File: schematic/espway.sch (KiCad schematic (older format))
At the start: 18 parts, among them M1 motor, M2 motor, U1 WS2812B, U2 AMS1117-5.0, U3 GY-521, U4 WS2812B, U5 WEMOS D1 mini, U6 L293D

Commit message: Add new schematic, update file structure and README
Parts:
- removed C1: 100n, symbol C
- removed C2: 1000u, symbol CP
- removed M1, M2: motor, symbol motor
- removed U1, U4: WS2812B, symbol ws2812b
- removed U2: AMS1117-5.0, symbol LM1117-5.0
- removed U3: GY-521, symbol GY-521
- removed U5: WEMOS D1 mini, symbol d1_mini
- removed U6: L293D, symbol L293D
- added BT1: 4.8V (4*AAA NiMH), symbol Battery
- added C1: 470u, symbol CP
- added C2: 100n, symbol C
- added J1, J2: CONN_01X02, symbol CONN_01X02
- added J3: CONN_01X04_MALE, symbol CONN_01X04_MALE
- added L1: Ferrite_Bead, symbol Ferrite_Bead
- added R10, R5, R6, R7, R8: 10k, symbol R
- added R11, R4: 470, symbol R
- added R9: 82k, symbol R
- added SW1: SW_Push, symbol SW_Push
- added U1: DRV8835, symbol DRV8835
- added U2: LM1117-3.3, symbol LM1117-3.3
- added U3: ESP-12E, symbol ESP-12E
- added U4: LSM6DS3, symbol LSM6DS3
- C5: value 1000u -> 100u
- R1: value 470 -> 10k
- R2: value 680k -> 10k
- R3: value 10k -> 470
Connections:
- net labels added: +3.3V, ADC, GPIO15, INT, SCL, SDA
- net labels removed: +5V, 1Y, 2Y, 3A, 4A
- wire segments 74 -> 72
- no-connect marks 1 -> 0
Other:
- note removed: "C6, C7 close to the motors\nMotor wires should be twisted pairs and as short as possible\nC1 close to U1 and U4\nC3, C4 close to U2\nC5 close to U5, C2 close to U6\nKeep wires between U3 and U5 short"

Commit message: Add kicad net file, begin associating footprints
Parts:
- BT1: footprint (none) -> Wire_Pads:SolderWirePad_2x_1-5mmDrill
- C1: footprint (none) -> Capacitors_SMD:CP_Elec_8x10
- C2, C3, C4, C6, C7: footprint (none) -> Capacitors_SMD:C_0603
- J3: footprint (none) -> Pin_Headers:Pin_Header_Angled_1x04_Pitch2.54mm
- L1: footprint (none) -> Inductors_SMD:L_0603
- R1, R10, R11, R2, R3, R4, R5, R6, R7, R8, R9: footprint (none) -> Resistors_SMD:R_0603
- U2: footprint (none) -> TO_SOT_Packages_SMD:SOT-223
- U3: footprint (none) -> ESP8266:ESP-12E_SMD
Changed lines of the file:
@@
 F 0 "U3" H 6200 2550 50  0000 C CNN
 F 1 "ESP-12E" H 6200 2750 50  0000 C CNN
-F 2 "" H 6200 2650 50  0001 C CNN
+F 2 "ESP8266:ESP-12E_SMD" H 6200 2650 50  0001 C CNN
 F 3 "" H 6200 2650 50  0001 C CNN
 	1    6200 2650
@@
 $EndComp
 $Comp
-L GND #PWR8
+L GND #PWR01
 U 1 1 59B6CE9D
 P 7450 3850
-F 0 "#PWR8" H 7450 3600 50  0001 C CNN
+F 0 "#PWR01" H 7450 3600 50  0001 C CNN
 F 1 "GND" H 7450 3700 50  0000 C CNN
 F 2 "" H 7450 3850 50  0001 C CNN
@@
 F 0 "R6" V 7530 3450 50  0000 C CNN
 F 1 "10k" V 7450 3450 50  0000 C CNN
-F 2 "" V 7380 3450 50  0001 C CNN
+F 2 "Resistors_SMD:R_0603" V 7380 3450 50  0001 C CNN
 F 3 "" H 7450 3450 50  0001 C CNN
 	1    7450 3450
@@
 F 0 "C4" H 5325 3550 50  0000 L CNN
 F 1 "100n" H 5325 3350 50  0000 L CNN
-F 2 "" H 5338 3300 50  0001 C CNN
+F 2 "Capacitors_SMD:C_0603" H 5338 3300 50  0001 C CNN
 F 3 "" H 5300 3450 50  0001 C CNN
 	1    5300 3450
@@
 F 0 "R3" V 7150 2300 50  0000 C CNN
 F 1 "470" V 7250 2350 50  0000 C CNN
-F 2 "" V 7180 2350 50  0001 C CNN
+F 2 "Resistors_SMD:R_0603" V 7180 2350 50  0001 C CNN
 F 3 "" H 7250 2350 50  0001 C CNN
 	1    7250 2350
@@
 F 0 "R4" V 7350 2600 50  0000 C CNN
 F 1 "470" V 7250 2450 50  0000 C CNN
-F 2 "" V 7180 2450 50  0001 C CNN
+F 2 "Resistors_SMD:R_0603" V 7180 2450 50  0001 C CNN
 F 3 "" H 7250 2450 50  0001 C CNN
 	1    7250 2450
@@
 F 0 "R1" V 5130 2350 50  0000 C CNN
 F 1 "10k" V 5050 2350 50  0000 C CNN
-F 2 "" V 4980 2350 50  0001 C CNN
+F 2 "Resistors_SMD:R_0603" V 4980 2350 50  0001 C CNN
 F 3 "" H 5050 2350 50  0001 C CNN
 	1    5050 2350
@@
 $EndComp
 $Comp
-L +3.3V #PWR4
+L +3.3V #PWR02
 U 1 1 59B80453
 P 4900 2250
-F 0 "#PWR4" H 4900 2100 50  0001 C CNN
+F 0 "#PWR02" H 4900 2100 50  0001 C CNN
 F 1 "+3.3V" H 4900 2390 50  0000 C CNN
 F 2 "" H 4900 2250 50  0001 C CNN
@@
 F 0 "R2" V 5130 2550 50  0000 C CNN
 F 1 "10k" V 5050 2550 50  0000 C CNN
-F 2 "" V 4980 2550 50  0001 C CNN
+F 2 "Resistors_SMD:R_0603" V 4980 2550 50  0001 C CNN
 F 3 "" H 5050 2550 50  0001 C CNN
 	1    5050 2550
@@
 F 0 "R9" V 9230 2200 50  0000 C CNN
 F 1 "82k" V 9150 2200 50  0000 C CNN
-F 2 "" V 9080 2200 50  0001 C CNN
+F 2 "Resistors_SMD:R_0603" V 9080 2200 50  0001 C CNN
 F 3 "" H 9150 2200 50  0001 C CNN
 	1    9150 2200
@@
 F 0 "R10" V 9230 2600 50  0000 C CNN
 F 1 "10k" V 9150 2600 50  0000 C CNN
-F 2 "" V 9080 2600 50  0001 C CNN
+F 2 "Resistors_SMD:R_0603" V 9080 2600 50  0001 C CNN
 F 3 "" H 9150 2600 50  0001 C CNN
 	1    9150 2600
@@
 $EndComp
 $Comp
-L GND #PWR15
+L GND #PWR03
 U 1 1 59B809EC
 P 9150 2850
-F 0 "#PWR15" H 9150 2600 50  0001 C CNN
+F 0 "#PWR03" H 9150 2600 50  0001 C CNN
 F 1 "GND" H 9150 2700 50  0000 C CNN
 F 2 "" H 9150 2850 50  0001 C CNN
@@
 SDA
 $Comp
-L +3.3V #PWR13
+L +3.3V #PWR04
 U 1 1 59B80D23
 P 8800 4000
-F 0 "#PWR13" H 8800 3850 50  0001 C CNN
+F 0 "#PWR04" H 8800 3850 50  0001 C CNN
 F 1 "+3.3V" H 8800 4140 50  0000 C CNN
 F 2 "" H 8800 4000 50  0001 C CNN
@@
 F 0 "R7" V 8880 4150 50  0000 C CNN
 F 1 "10k" V 8800 4150 50  0000 C CNN
-F 2 "" V 8730 4150 50  0001 C CNN
+F 2 "Resistors_SMD:R_0603" V 8730 4150 50  0001 C CNN
 F 3 "" H 8800 4150 50  0001 C CNN
 	1    8800 4150
@@
 F 0 "R8" V 9080 4150 50  0000 C CNN
 F 1 "10k" V 9000 4150 50  0000 C CNN
-F 2 "" V 8930 4150 50  0001 C CNN
+F 2 "Resistors_SMD:R_0603" V 8930 4150 50  0001 C CNN
 F 3 "" H 9000 4150 50  0001 C CNN
 	1    9000 4150
@@
 SDA
 $Comp
-L GND #PWR11
+L GND #PWR05
 U 1 1 59B8139A
 P 8050 2750
-F 0 "#PWR11" H 8050 2500 50  0001 C CNN
+F 0 "#PWR05" H 8050 2500 50  0001 C CNN
 F 1 "GND" H 8050 2600 50  0000 C CNN
 F 2 "" H 8050 2750 50  0001 C CNN
@@
 F 0 "R11" V 9580 4550 50  0000 C CNN
 F 1 "470" V 9500 4550 50  0000 C CNN
-F 2 "" V 9430 4550 50  0001 C CNN
+F 2 "Resistors_SMD:R_0603" V 9430 4550 50  0001 C CNN
 F 3 "" H 9500 4550 50  0001 C CNN
 	1    9500 4550
@@
 F 0 "U2" H 5950 950 50  0000 C CNN
 F 1 "LM1117-3.3" H 5850 1450 50  0000 C CNN
-F 2 "" H 5850 1200 50  0001 C CNN
+F 2 "TO_SOT_Packages_SMD:SOT-223" H 5850 1200 50  0001 C CNN
 F 3 "" H 5850 1200 50  0001 C CNN
 	1    5850 1200
@@
 $EndComp
 $Comp
-L GND #PWR6
+L GND #PWR06
 U 1 1 59B829FA
 P 5850 1600
-F 0 "#PWR6" H 5850 1350 50  0001 C CNN
+F 0 "#PWR06" H 5850 1350 50  0001 C CNN
 F 1 "GND" H 5850 1450 50  0000 C CNN
 F 2 "" H 5850 1600 50  0001 C CNN
@@
 $EndComp
 $Comp
-L +3.3V #PWR7
+L +3.3V #PWR07
 U 1 1 59B82E61
 P 6300 1200
-F 0 "#PWR7" H 6300 1050 50  0001 C CNN
+F 0 "#PWR07" H 6300 1050 50  0001 C CNN
 F 1 "+3.3V" H 6300 1340 50  0000 C CNN
 F 2 "" H 6300 1200 50  0001 C CNN
@@
 F 0 "C6" H 8275 5900 50  0000 L CNN
 F 1 "100n" H 8275 5700 50  0000 L CNN
-F 2 "" H 8288 5650 50  0001 C CNN
+F 2 "Capacitors_SMD:C_0603" H 8288 5650 50  0001 C CNN
 F 3 "" H 8250 5800 50  0001 C CNN
 	1    8250 5800
@@
 $EndComp
 $Comp
-L GND #PWR12
+L GND #PWR08
 U 1 1 59B83CEA
 P 8600 6150
-F 0 "#PWR12" H 8600 5900 50  0001 C CNN
+F 0 "#PWR08" H 8600 5900 50  0001 C CNN
 F 1 "GND" H 8600 6000 50  0000 C CNN
 F 2 "" H 8600 6150 50  0001 C CNN
@@
 F 0 "L1" V 7750 5825 50  0000 C CNN
 F 1 "Ferrite_Bead" V 8050 5800 50  0000 C CNN
-F 2 "" V 7830 5800 50  0001 C CNN
+F 2 "Inductors_SMD:L_0603" V 7830 5800 50  0001 C CNN
 F 3 "" H 7900 5800 50  0001 C CNN
 	1    7900 5800
@@
 F 0 "C7" H 8275 6300 50  0000 L CNN
 F 1 "100n" H 8275 6100 50  0000 L CNN
-F 2 "" H 8288 6050 50  0001 C CNN
+F 2 "Capacitors_SMD:C_0603" H 8288 6050 50  0001 C CNN
 F 3 "" H 8250 6200 50  0001 C CNN
 	1    8250 6200
@@
 $EndComp
 $Comp
-L GND #PWR16
+L GND #PWR09
 U 1 1 59B849E7
 P 9700 5250
-F 0 "#PWR16" H 9700 5000 50  0001 C CNN
+F 0 "#PWR09" H 9700 5000 50  0001 C CNN
 F 1 "GND" H 9700 5100 50  0000 C CNN
 F 2 "" H 9700 5250 50  0001 C CNN
@@
 INT
 $Comp
-L +3.3V #PWR10
+L +3.3V #PWR010
 U 1 1 59B9046E
 P 7650 4550
-F 0 "#PWR10" H 7650 4400 50  0001 C CNN
+F 0 "#PWR010" H 7650 4400 50  0001 C CNN
 F 1 "+3.3V" H 7650 4690 50  0000 C CNN
 F 2 "" H 7650 4550 50  0001 C CNN
@@
 F 0 "J3" H 8350 2725 50  0000 C CNN
 F 1 "CONN_01X04_MALE" H 8350 1950 50  0000 C CNN
-F 2 "" H 8350 2650 50  0001 C CNN
+F 2 "Pin_Headers:Pin_Header_Angled_1x04_Pitch2.54mm" H 8350 2650 50  0001 C CNN
 F 3 "" H 8350 2650 50  0001 C CNN
 	1    8350 2350
@@
 F 0 "C2" H 2775 2100 50  0000 L CNN
 F 1 "100n" H 2775 1900 50  0000 L CNN
-F 2 "" H 2788 1850 50  0001 C CNN
+F 2 "Capacitors_SMD:C_0603" H 2788 1850 50  0001 C CNN
 F 3 "" H 2750 2000 50  0001 C CNN
 	1    2750 2000
@@
 F 0 "C3" H 4225 2100 50  0000 L CNN
 F 1 "100n" H 4225 1900 50  0000 L CNN
-F 2 "" H 4238 1850 50  0001 C CNN
+F 2 "Capacitors_SMD:C_0603" H 4238 1850 50  0001 C CNN
 F 3 "" H 4200 2000 50  0001 C CNN
 	1    4200 2000
@@
 F 0 "C1" H 2525 2100 50  0000 L CNN
 F 1 "470u" H 2525 1900 50  0000 L CNN
-F 2 "" H 2538 1850 50  0001 C CNN
+F 2 "Capacitors_SMD:CP_Elec_8x10" H 2538 1850 50  0001 C CNN
 F 3 "" H 2500 2000 50  0001 C CNN
 	1    2500 2000
@@
 $EndComp
 $Comp
-L GND #PWR3
+L GND #PWR011
 U 1 1 59BA4FB0
 P 4500 1850
-F 0 "#PWR3" H 4500 1600 50  0001 C CNN
+F 0 "#PWR011" H 4500 1600 50  0001 C CNN
 F 1 "GND" H 4500 1700 50  0000 C CNN
 F 2 "" H 4500 1850 50  0001 C CNN
@@
 GPIO15
 $Comp
-L GND #PWR2
+L GND #PWR012
 U 1 1 59BA5B49
 P 2750 3200
-F 0 "#PWR2" H 2750 2950 50  0001 C CNN
+F 0 "#PWR012" H 2750 2950 50  0001 C CNN
 F 1 "GND" H 2750 3050 50  0000 C CNN
 F 2 "" H 2750 3200 50  0001 C CNN
@@
 F 0 "BT1" H 5100 1500 50  0000 L CNN
 F 1 "4.8V (4*AAA NiMH)" H 5100 1400 50  0000 L CNN
-F 2 "" V 5000 1460 50  0001 C CNN
+F 2 "Wire_Pads:SolderWirePad_2x_1-5mmDrill" V 5000 1460 50  0001 C CNN
 F 3 "" V 5000 1460 50  0001 C CNN
 	1    5000 1400
@@
 Connection ~ 2500 2350
 $Comp
-L +BATT #PWR5
+L +BATT #PWR013
 U 1 1 59BA76F1
 P 5000 1050
-F 0 "#PWR5" H 5000 900 50  0001 C CNN
+F 0 "#PWR013" H 5000 900 50  0001 C CNN
 F 1 "+BATT" H 5000 1190 50  0000 C CNN
 F 2 "" H 5000 1050 50  0001 C CNN
@@
 	5000 1200 5550 1200
 $Comp
-L +BATT #PWR14
+L +BATT #PWR014
 U 1 1 59BA7893
 P 9150 1800
-F 0 "#PWR14" H 9150 1650 50  0001 C CNN
+F 0 "#PWR014" H 9150 1650 50  0001 C CNN
 F 1 "+BATT" H 9150 1940 50  0000 C CNN
 F 2 "" H 9150 1800 50  0001 C CNN
@@
 $EndComp
 $Comp
-L +BATT #PWR1
+L +BATT #PWR015
 U 1 1 59BA7C2C
 P 2300 2350
-F 0 "#PWR1" H 2300 2200 50  0001 C CNN
+F 0 "#PWR015" H 2300 2200 50  0001 C CNN
 F 1 "+BATT" H 2300 2490 50  0000 C CNN
 F 2 "" H 2300 2350 50  0001 C CNN
@@
 F 0 "R5" V 7150 3000 50  0000 C CNN
 F 1 "10k" V 7250 2850 50  0000 C CNN
-F 2 "" V 7180 2850 50  0001 C CNN
+F 2 "Resistors_SMD:R_0603" V 7180 2850 50  0001 C CNN
 F 3 "" H 7250 2850 50  0001 C CNN
 	1    7250 2850
@@
 $EndComp
 $Comp
-L +3.3V #PWR9
+L +3.3V #PWR016
 U 1 1 59BB0EE7
 P 7600 2850
-F 0 "#PWR9" H 7600 2700 50  0001 C CNN
+F 0 "#PWR016" H 7600 2700 50  0001 C CNN
 F 1 "+3.3V" H 7600 2990 50  0000 C CNN
 F 2 "" H 7600 2850 50  0001 C CNN

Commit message: Updates to schematic
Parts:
- BT1: footprint Wire_Pads:SolderWirePad_2x_1-5mmDrill -> Wire_Connections_Bridges:WireConnection_1.20mmDrill
- C5: footprint (none) -> Capacitors_SMD:CP_Elec_6.3x5.8
- J1, J2: footprint (none) -> Wire_Connections_Bridges:WireConnection_1.20mmDrill
- SW1: footprint (none) -> Buttons_Switches_SMD:SW_SPST_KMR2
- U1: footprint (none) -> espway-modules:WSON-12
- U4: footprint (none) -> espway-modules:LGA-14L
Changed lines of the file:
@@
 F 0 "SW1" H 9550 5000 50  0000 L CNN
 F 1 "SW_Push" H 9500 4840 50  0000 C CNN
-F 2 "" H 9500 5100 50  0001 C CNN
+F 2 "Buttons_Switches_SMD:SW_SPST_KMR2" H 9500 5100 50  0001 C CNN
 F 3 "" H 9500 5100 50  0001 C CNN
 	1    9500 4900
@@
 F 0 "U4" H 9250 6500 60  0000 C CNN
 F 1 "LSM6DS3" V 8800 6900 60  0000 C CNN
-F 2 "" H 8800 6150 60  0001 C CNN
+F 2 "espway-modules:LGA-14L" H 8800 6150 60  0001 C CNN
 F 3 "" H 8800 6150 60  0001 C CNN
 	1    8800 6150
@@
 F 0 "C5" H 6225 1550 50  0000 L CNN
 F 1 "100u" H 6225 1350 50  0000 L CNN
-F 2 "" H 6238 1300 50  0001 C CNN
+F 2 "Capacitors_SMD:CP_Elec_6.3x5.8" H 6238 1300 50  0001 C CNN
 F 3 "" H 6200 1450 50  0001 C CNN
 	1    6200 1450
@@
 F 0 "U1" H 3050 4250 60  0000 C CNN
 F 1 "DRV8835" H 3500 4000 60  0000 C CNN
-F 2 "" H 3500 3050 60  0001 C CNN
+F 2 "espway-modules:WSON-12" H 3500 3050 60  0001 C CNN
 F 3 "" H 3500 3050 60  0001 C CNN
 	1    3450 3200
@@
 F 0 "BT1" H 5100 1500 50  0000 L CNN
 F 1 "4.8V (4*AAA NiMH)" H 5100 1400 50  0000 L CNN
-F 2 "Wire_Pads:SolderWirePad_2x_1-5mmDrill" V 5000 1460 50  0001 C CNN
+F 2 "Wire_Connections_Bridges:WireConnection_1.20mmDrill" V 5000 1460 50  0001 C CNN
 F 3 "" V 5000 1460 50  0001 C CNN
 	1    5000 1400
@@
 F 0 "J1" H 1900 2700 50  0000 C CNN
 F 1 "CONN_01X02" V 2000 2550 50  0000 C CNN
-F 2 "" H 1900 2550 50  0001 C CNN
+F 2 "Wire_Connections_Bridges:WireConnection_1.20mmDrill" H 1900 2550 50  0001 C CNN
 F 3 "" H 1900 2550 50  0001 C CNN
 	1    1900 2550
@@
 F 0 "J2" H 2200 3050 50  0000 C CNN
 F 1 "CONN_01X02" V 2300 2900 50  0000 C CNN
-F 2 "" H 2200 2900 50  0001 C CNN
+F 2 "Wire_Connections_Bridges:WireConnection_1.20mmDrill" H 2200 2900 50  0001 C CNN
 F 3 "" H 2200 2900 50  0001 C CNN
 	1    2200 2900

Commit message: Update schematic and PCB layout
Misses power led and routing
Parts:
- U2: symbol LM1117-3.3 -> LM1117-3.3-RESCUE-espway
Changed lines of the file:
@@
 EESchema Schematic File Version 2
+LIBS:espway-rescue
 LIBS:power
 LIBS:device
@@
 $EndComp
 $Comp
-L LM1117-3.3 U2
+L LM1117-3.3-RESCUE-espway U2
 U 1 1 59B82983
 P 5850 1200

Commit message: Schematic and PCB update
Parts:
- added D?: LED, symbol LED
- added R?: 470, symbol R
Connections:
- net +3V3: now also R?.2
- net GND: now also D?.1 (K)
- new net: D?.2 (A), R?.1
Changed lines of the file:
@@
 L +3.3V #PWR07
 U 1 1 59B82E61
-P 6300 1200
-F 0 "#PWR07" H 6300 1050 50  0001 C CNN
-F 1 "+3.3V" H 6300 1340 50  0000 C CNN
-F 2 "" H 6300 1200 50  0001 C CNN
-F 3 "" H 6300 1200 50  0001 C CNN
-	1    6300 1200
+P 6200 1200
+F 0 "#PWR07" H 6200 1050 50  0001 C CNN
+F 1 "+3.3V" H 6200 1340 50  0000 C CNN
+F 2 "" H 6200 1200 50  0001 C CNN
+F 3 "" H 6200 1200 50  0001 C CNN
+	1    6200 1200
 	1    0    0    -1
 $EndComp
@@
 	5850 1600 5850 1500
 Wire Wire Line
-	6300 1200 6150 1200
-Wire Wire Line
 	8250 5650 8250 5550
 Wire Wire Line
@@
 Wire Wire Line
 	6200 1300 6200 1200
-Connection ~ 6200 1200
-Wire Wire Line
-	5000 1600 6200 1600
+Wire Wire Line
+	5000 1600 6750 1600
 Wire Wire Line
 	2500 1850 4500 1850
@@
 Wire Wire Line
 	2750 2850 2750 2800
+$Comp
+L R R?
+U 1 1 59BE998C
+P 6550 1200
+F 0 "R?" V 6630 1200 50  0000 C CNN
+F 1 "470" V 6550 1200 50  0000 C CNN
+F 2 "" V 6480 1200 50  0001 C CNN
+F 3 "" H 6550 1200 50  0001 C CNN
+	1    6550 1200
+	0    1    1    0
+$EndComp
+$Comp
+L LED D?
+U 1 1 59BE99F7
+P 6750 1400
+F 0 "D?" H 6750 1500 50  0000 C CNN
+F 1 "LED" H 6750 1300 50  0000 C CNN
+F 2 "" H 6750 1400 50  0001 C CNN
+F 3 "" H 6750 1400 50  0001 C CNN
+	1    6750 1400
+	0    -1   -1   0
+$EndComp
+Wire Wire Line
+	6150 1200 6400 1200
+Connection ~ 6200 1200
+Wire Wire Line
+	6700 1200 6750 1200
+Wire Wire Line
+	6750 1200 6750 1250
+Wire Wire Line
+	6750 1600 6750 1550
+Connection ~ 6200 1600
 $EndSCHEMATC

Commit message: Update schematic and PCB
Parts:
- D1: renamed from D?; footprint (none) -> LEDs:LED_0603
- R12: renamed from R?; footprint (none) -> Resistors_SMD:R_0603
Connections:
- net at R3.1: now also J3.2; no longer J3.3
- net at R4.1: now also J3.3; no longer J3.2
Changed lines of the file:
@@
 	8050 2750 8050 2650
-Wire Wire Line
-	7400 2450 8050 2450
 Wire Wire Line
 	5850 1600 5850 1500
@@
 Connection ~ 2750 2350
 Connection ~ 5000 1200
-Wire Wire Line
-	7400 2350 7400 2250
-Wire Wire Line
-	7400 2250 8050 2250
 $Comp
 L R R5
@@
 	2750 2850 2750 2800
 $Comp
-L R R?
+L R R12
 U 1 1 59BE998C
 P 6550 1200
-F 0 "R?" V 6630 1200 50  0000 C CNN
+F 0 "R12" V 6630 1200 50  0000 C CNN
 F 1 "470" V 6550 1200 50  0000 C CNN
-F 2 "" V 6480 1200 50  0001 C CNN
+F 2 "Resistors_SMD:R_0603" V 6480 1200 50  0001 C CNN
 F 3 "" H 6550 1200 50  0001 C CNN
 	1    6550 1200
@@
 $EndComp
 $Comp
-L LED D?
+L LED D1
 U 1 1 59BE99F7
 P 6750 1400
-F 0 "D?" H 6750 1500 50  0000 C CNN
+F 0 "D1" H 6750 1500 50  0000 C CNN
 F 1 "LED" H 6750 1300 50  0000 C CNN
-F 2 "" H 6750 1400 50  0001 C CNN
+F 2 "LEDs:LED_0603" H 6750 1400 50  0001 C CNN
 F 3 "" H 6750 1400 50  0001 C CNN
 	1    6750 1400
@@
 	6750 1600 6750 1550
 Connection ~ 6200 1600
+Wire Wire Line
+	7400 2450 7900 2450
+Wire Wire Line
+	7900 2450 7900 2250
+Wire Wire Line
+	7900 2250 8050 2250
+Wire Wire Line
+	7400 2350 8050 2350
+Wire Wire Line
+	8050 2350 8050 2450
 $EndSCHEMATC

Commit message: Update PCB
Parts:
- BT1, J1, J2: footprint Wire_Connections_Bridges:WireConnection_1.20mmDrill -> Wire_Connections_Bridges:WireConnection_1.00mmDrill
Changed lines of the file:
@@
 F 0 "BT1" H 5100 1500 50  0000 L CNN
 F 1 "4.8V (4*AAA NiMH)" H 5100 1400 50  0000 L CNN
-F 2 "Wire_Connections_Bridges:WireConnection_1.20mmDrill" V 5000 1460 50  0001 C CNN
+F 2 "Wire_Connections_Bridges:WireConnection_1.00mmDrill" V 5000 1460 50  0001 C CNN
 F 3 "" V 5000 1460 50  0001 C CNN
 	1    5000 1400
@@
 F 0 "J1" H 1900 2700 50  0000 C CNN
 F 1 "CONN_01X02" V 2000 2550 50  0000 C CNN
-F 2 "Wire_Connections_Bridges:WireConnection_1.20mmDrill" H 1900 2550 50  0001 C CNN
+F 2 "Wire_Connections_Bridges:WireConnection_1.00mmDrill" H 1900 2550 50  0001 C CNN
 F 3 "" H 1900 2550 50  0001 C CNN
 	1    1900 2550
@@
 F 0 "J2" H 2200 3050 50  0000 C CNN
 F 1 "CONN_01X02" V 2300 2900 50  0000 C CNN
-F 2 "Wire_Connections_Bridges:WireConnection_1.20mmDrill" H 2200 2900 50  0001 C CNN
+F 2 "Wire_Connections_Bridges:WireConnection_1.00mmDrill" H 2200 2900 50  0001 C CNN
 F 3 "" H 2200 2900 50  0001 C CNN
 	1    2200 2900

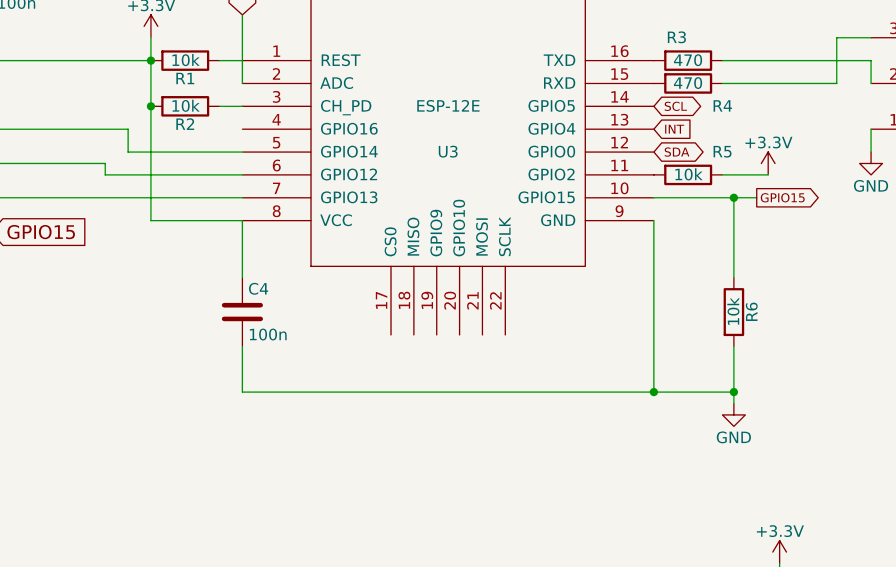
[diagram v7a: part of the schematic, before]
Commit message: Plenty of updates to PCB
* Fix bug where one motor would spin in bootloader
* Add helpful labels
* Add another via for V+ near motor driver
* Larger screw holes
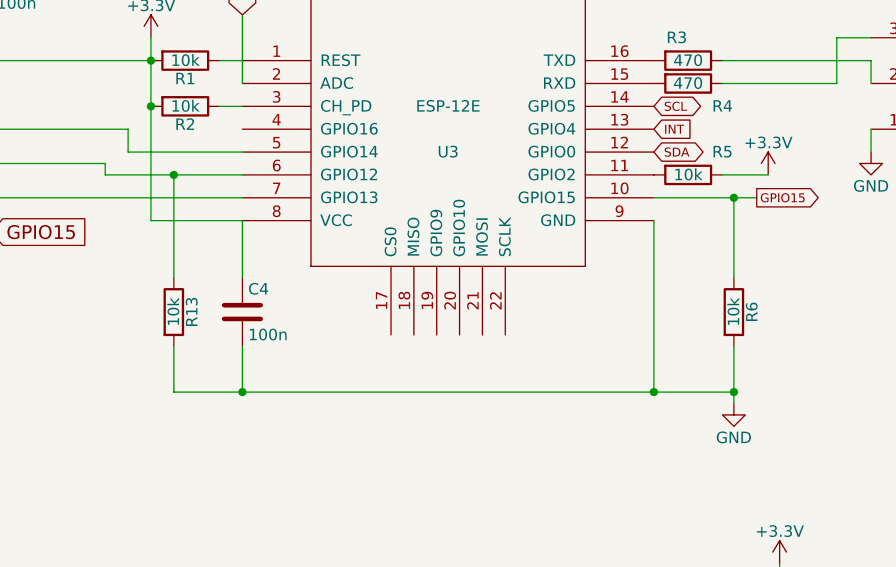
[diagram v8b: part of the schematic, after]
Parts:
- added R13: 10k, Resistors_SMD:R_0603, symbol R
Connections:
- net GND: now also R13.2
- net at U1.9 (AIN2/AENBL), U3.6 (GPIO12): now also R13.1
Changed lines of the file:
@@
 	9500 5550 9350 5550
 Wire Wire Line
-	5300 3800 7450 3800
+	5000 3800 7450 3800
 Wire Wire Line
 	6200 1300 6200 1200
@@
 Wire Wire Line
 	8050 2350 8050 2450
+$Comp
+L R R13
+U 1 1 59E13532
+P 5000 3450
+F 0 "R13" V 5080 3450 50  0000 C CNN
+F 1 "10k" V 5000 3450 50  0000 C CNN
+F 2 "Resistors_SMD:R_0603" V 4930 3450 50  0001 C CNN
+F 3 "" H 5000 3450 50  0001 C CNN
+	1    5000 3450
+	1    0    0    -1
+$EndComp
+Wire Wire Line
+	5000 3300 5000 2850
+Connection ~ 5000 2850
+Wire Wire Line
+	5000 3600 5000 3800
+Connection ~ 5300 3800
 $EndSCHEMATC
